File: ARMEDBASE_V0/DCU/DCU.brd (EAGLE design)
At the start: 86.3 x 69.5 mm, 35 parts, among them IC2 MEGA8-P, Q1 16Mhz, Q2 2N3904, Q3 2N3904

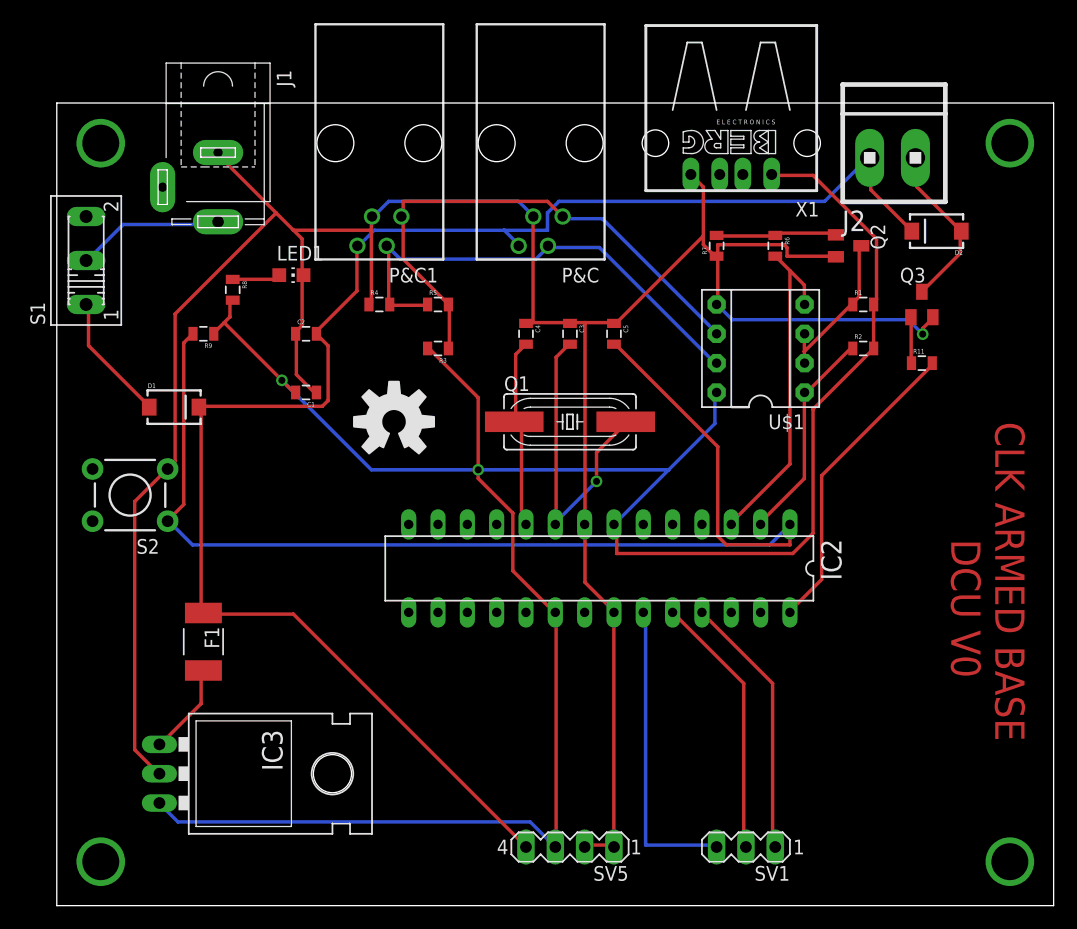
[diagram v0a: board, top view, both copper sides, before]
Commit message: DCU
DCU seperation and CNC settings update for another shot.
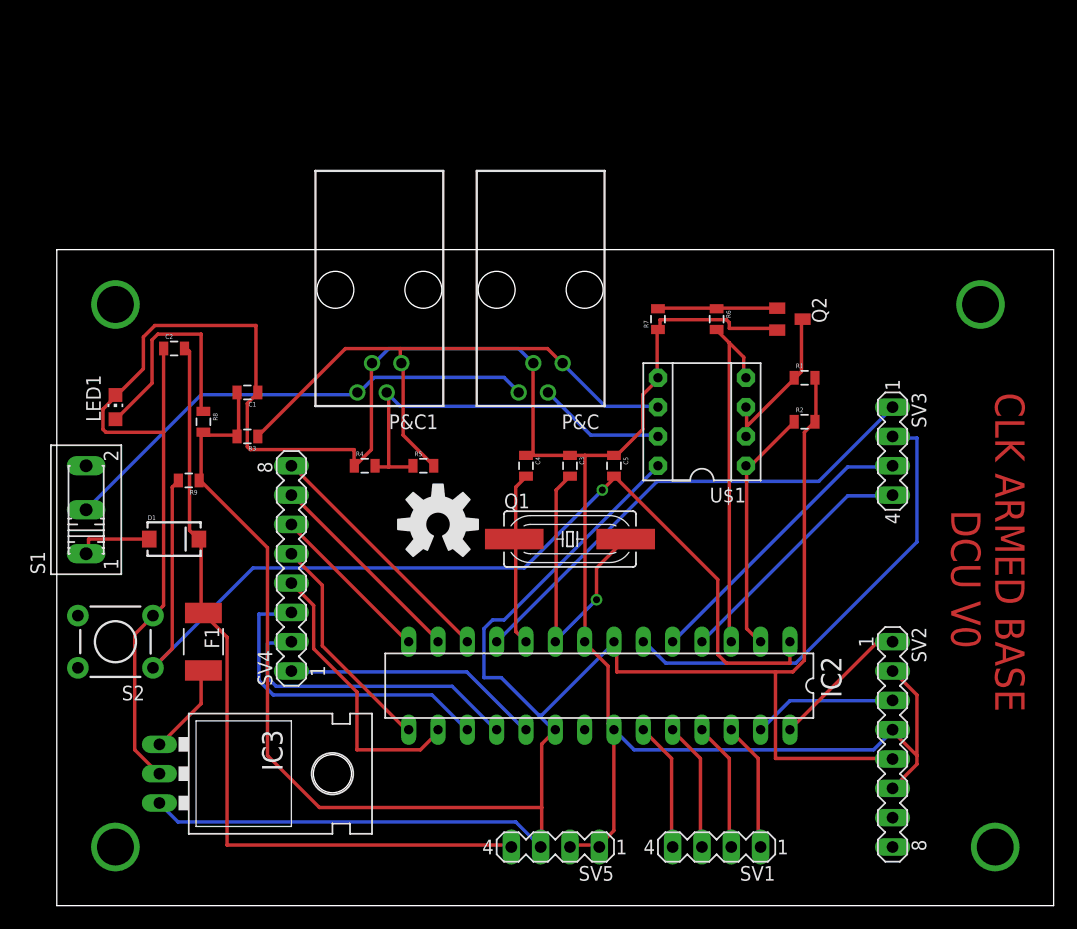
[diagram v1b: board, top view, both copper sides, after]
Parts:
- removed D2: (no value), SparkFun-DiscreteSemi:SMA-DIODE
- removed J1: (no value), con-jack:SPC4078
- removed J2: (no value), con-amp:1X2MTA
- removed Q3: 2N3904, semicon-smd-ipc:SOT23
- removed R11: 1K, SparkFun-Passives:0805
- removed X1: (no value), con-berg:PN87520
- added SV2, SV4: (no value), con-lstb:MA08-1
- added SV3: 5v, con-lstb:MA04-1
- SV1: device con-lstb:MA03-1 -> con-lstb:MA04-1
- moved S1 21.6 mm to (2.54, 34.3)
- moved LED1 19.1 mm to (5.08, 43.2), turned to 0 degrees
- moved R3 18.2 mm to (16.5, 40.6)
- moved R4 14.0 mm to (26.7, 38.1)
- moved R5 14.0 mm to (31.8, 38.1)
- moved R9 12.8 mm to (11.4, 36.8)
- moved S2 12.8 mm to (5.08, 22.9)
- moved P&C 12.7 mm to (41.9, 53.3)
- moved P&C1 12.7 mm to (27.9, 53.3)
- moved R8 11.7 mm to (12.7, 41.9)
- moved C2 11.5 mm to (10.2, 48.3)
- moved C3 11.4 mm to (44.5, 38.1)
- moved C4 11.4 mm to (40.6, 38.1)
- moved C5 11.4 mm to (48.3, 38.1)
- moved D1 11.4 mm to (10.2, 31.8)
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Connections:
- removed net N$6: Q3.1, R11.1
- removed net N$9: IC2.28, R11.2
- new net KP1: IC2.19, SV4.1
- new net KP2: IC2.18, SV4.2
- new net KP3: IC2.17, SV4.3
- new net KP4: IC2.16, SV4.4
- new net KP5: IC2.15, SV4.5
- new net KP6: IC2.14, SV4.6
- new net KP7: IC2.13, SV4.7
- new net KP8: IC2.12, SV4.8
- new net LCDD4: IC2.4, SV3.4
- new net LCDD5: IC2.5, SV3.3
- new net LCDD6: IC2.6, SV3.2
- new net LCDD7: IC2.11, SV3.1
- net GND: now also SV2.2, SV2.4, SV2.6; no longer J1.1, Q3.2, X1.4
- net LCDEN: now also IC2.28, SV2.1; no longer IC2.27
- net LCDRS: now also IC2.27, SV2.3; no longer IC2.26
- net N$15: now also SV1.2; no longer SV1.1
- net N$16: now also SV1.3; no longer SV1.2
- net N$17: now also SV1.4; no longer SV1.3
- net N$5: now also IC2.26, SV1.1; no longer D2.A, J2.1, Q3.3
- net VCC: now also P&C.4, P&C1.4; no longer J1.3
- net VCC12V: no longer D2.C, J2.2, P&C.4, P&C1.4
- net VCC5V: now also SV2.5; no longer X1.1
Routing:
- net VCC12V: track 139.2 -> 69.5 mm
- net LCDD7: track 0.00 -> 42.7 mm
- net LCDD6: track 0.00 -> 40.0 mm
- net VCC: track 12.8 -> 42.8 mm
- net KP3: track 0.00 -> 28.5 mm
- net KP2: track 0.00 -> 26.8 mm
- net N$9: track 26.7 -> 0.00 mm
- net LCDD5: track 0.00 -> 25.3 mm
- net KP4: track 0.00 -> 24.7 mm
- net KP1: track 0.00 -> 22.4 mm
- net LCDD4: track 0.00 -> 21.8 mm
- net KP8: track 0.00 -> 21.6 mm
- net KP5: track 0.00 -> 19.6 mm
- net KP7: track 0.00 -> 18.0 mm
- net N$17: track 26.5 -> 11.2 mm
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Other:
- board size 86.3 x 69.5 mm -> 86.3 x 56.8 mm
